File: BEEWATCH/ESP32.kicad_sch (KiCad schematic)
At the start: 34 parts, among them U4 W25Q128JVS

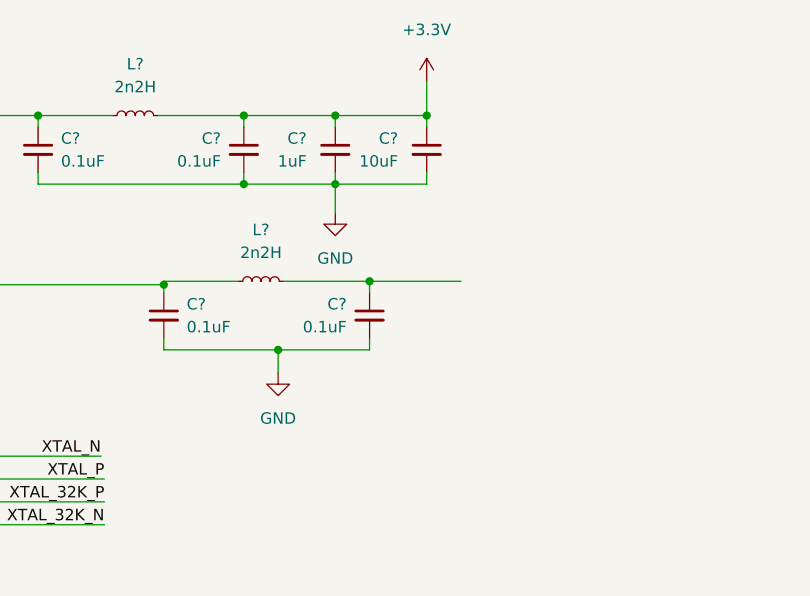
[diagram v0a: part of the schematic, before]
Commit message: Inverted F Antenna designed
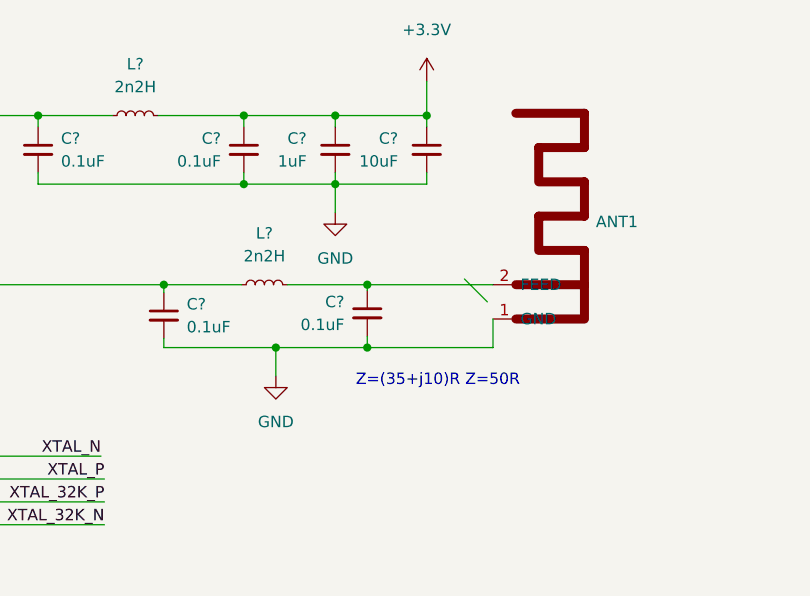
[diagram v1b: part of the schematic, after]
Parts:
- added ANT1: ~, Project:IFA_2.4GHz, symbol Project_Library:IFA_2.4GHz
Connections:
- net GND: now also ANT1.1 (GND)
- net at C?.1, L?.2: now also ANT1.2 (FEED)
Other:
- note added: "Z=(35+j10)R Z=50R"
- moved on the sheet: L?
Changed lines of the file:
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@@
   (junction (at 164.084 49.149) (diameter 0) (color 0 0 0 0)
   )
+  (junction (at 294.64 67.945) (diameter 0) (color 0 0 0 0)
+  )
   (junction (at 301.244 49.149) (diameter 0) (color 0 0 0 0)
   )
   (junction (at 258.064 49.149) (diameter 0) (color 0 0 0 0)
   )
+  (junction (at 294.64 74.93) (diameter 0) (color 0 0 0 0)
+  )
   (junction (at 355.854 225.171) (diameter 0) (color 0 0 0 0)
   )
@@
   (junction (at 58.42 120.015) (diameter 0) (color 0 0 0 0)
   )
+  (junction (at 284.48 74.93) (diameter 0) (color 0 0 0 0)
+  )
   (junction (at 349.25 206.756) (diameter 0) (color 0 0 0 0)
   )
@@
   (junction (at 234.95 49.149) (diameter 0) (color 0 0 0 0)
   )
-  (junction (at 294.894 67.564) (diameter 0) (color 0 0 0 0)
-  )
   (junction (at 184.404 49.149) (diameter 0) (color 0 0 0 0)
   )
@@
   (junction (at 280.924 49.149) (diameter 0) (color 0 0 0 0)
   )
-  (junction (at 284.734 75.184) (diameter 0) (color 0 0 0 0)
-  )
   (junction (at 58.42 114.935) (diameter 0) (color 0 0 0 0)
   )
@@
   (junction (at 174.244 49.149) (diameter 0) (color 0 0 0 0)
   )
+  (bus_entry (at 305.435 67.31) (size 2.54 2.54)
+    (stroke (width 0) (type default))
+  )
   (wire (pts (xy 223.52 127.635) (xy 223.52 125.095))
     (stroke (width 0) (type default))
@@
     (stroke (width 0) (type default))
   )
-  (wire (pts (xy 272.034 67.945) (xy 272.034 67.564))
-    (stroke (width 0) (type default))
-  )
   (wire (pts (xy 214.63 49.149) (xy 214.63 55.245))
     (stroke (width 0) (type default))
   )
-  (wire (pts (xy 294.894 68.834) (xy 294.894 67.564))
-    (stroke (width 0) (type default))
-  )
   (wire (pts (xy 183.515 71.755) (xy 192.405 71.755))
     (stroke (width 0) (type default))
@@
     (stroke (width 0) (type default))
   )
-  (wire (pts (xy 284.734 75.184) (xy 272.034 75.184))
-    (stroke (width 0) (type default))
-  )
   (wire (pts (xy 280.924 56.769) (xy 280.924 55.499))
     (stroke (width 0) (type default))
@@
     (stroke (width 0) (type default))
   )
+  (wire (pts (xy 308.61 74.93) (xy 294.64 74.93))
+    (stroke (width 0) (type default))
+  )
   (wire (pts (xy 349.885 170.815) (xy 349.885 179.07))
     (stroke (width 0) (type default))
@@
     (stroke (width 0) (type default))
   )
-  (wire (pts (xy 272.034 73.914) (xy 272.034 75.184))
+  (wire (pts (xy 272.034 73.914) (xy 272.034 74.93))
     (stroke (width 0) (type default))
   )
@@
     (stroke (width 0) (type default))
   )
-  (wire (pts (xy 284.734 75.184) (xy 284.734 77.724))
-    (stroke (width 0) (type default))
-  )
-  (wire (pts (xy 305.054 67.564) (xy 294.894 67.564))
+  (wire (pts (xy 284.48 74.93) (xy 284.48 78.105))
+    (stroke (width 0) (type default))
+  )
+  (wire (pts (xy 294.64 67.945) (xy 308.61 67.945))
     (stroke (width 0) (type default))
   )
@@
     (stroke (width 0) (type default))
   )
-  (wire (pts (xy 272.034 67.564) (xy 280.289 67.564))
+  (wire (pts (xy 272.034 67.945) (xy 280.67 67.945))
     (stroke (width 0) (type default))
   )
@@
     (stroke (width 0) (type default))
   )
-  (wire (pts (xy 294.894 67.564) (xy 285.369 67.564))
-    (stroke (width 0) (type default))
-  )
   (wire (pts (xy 197.485 66.675) (xy 198.12 66.675))
     (stroke (width 0) (type default))
@@
     (stroke (width 0) (type default))
   )
-  (wire (pts (xy 294.894 75.184) (xy 284.734 75.184))
+  (wire (pts (xy 294.64 74.93) (xy 284.48 74.93))
     (stroke (width 0) (type default))
   )
@@
     (stroke (width 0) (type default))
   )
+  (wire (pts (xy 308.61 71.755) (xy 308.61 74.93))
+    (stroke (width 0) (type default))
+  )
   (wire (pts (xy 361.95 183.515) (xy 361.95 189.103))
     (stroke (width 0) (type default))
@@
     (stroke (width 0) (type default))
   )
+  (wire (pts (xy 294.64 67.945) (xy 285.75 67.945))
+    (stroke (width 0) (type default))
+  )
   (wire (pts (xy 349.885 189.103) (xy 356.743 189.103))
     (stroke (width 0) (type default))
@@
     (stroke (width 0) (type default))
   )
-  (wire (pts (xy 294.894 75.184) (xy 294.894 73.914))
+  (wire (pts (xy 294.64 73.66) (xy 294.64 74.93))
+    (stroke (width 0) (type default))
+  )
+  (wire (pts (xy 294.64 67.945) (xy 294.64 68.58))
     (stroke (width 0) (type default))
   )
@@
   )
   (wire (pts (xy 280.924 56.769) (xy 258.064 56.769))
+    (stroke (width 0) (type default))
+  )
+  (wire (pts (xy 284.48 74.93) (xy 272.034 74.93))
     (stroke (width 0) (type default))
   )
@@
     (effects (font (size 1.27 1.27)) (justify left bottom))
   )
+  (text "Z=(35+j10)R Z=50R\n" (at 293.37 79.375 0)
+    (effects (font (size 1.27 1.27)) (justify left bottom))
+  )
   (label "SPI_D0" (at 183.515 69.215 0) (fields_autoplaced)
     (effects (font (size 1.27 1.27)) (justify left bottom))
@@
     (effects (font (size 1.27 1.27)) (justify right))
   )
-  (symbol (lib_id "Device:C_Small") (at 294.894 71.374 0) (mirror y) (unit 1)
-    (in_bom yes) (on_board yes) (dnp no) (fields_autoplaced)
-    (property "Reference" "C?" (at 292.354 70.1102 0)
-      (effects (font (size 1.27 1.27)) (justify left))
-    )
-    (property "Value" "0.1uF" (at 292.354 72.6502 0)
-      (effects (font (size 1.27 1.27)) (justify left))
-    )
-    (property "Footprint" "" (at 294.894 71.374 0)
-      (effects (font (size 1.27 1.27)) hide)
-    )
-    (property "Datasheet" "~" (at 294.894 71.374 0)
+  (symbol (lib_id "Device:C_Small") (at 294.64 71.12 0) (mirror y) (unit 1)
+    (in_bom yes) (on_board yes) (dnp no) (fields_autoplaced)
+    (property "Reference" "C?" (at 292.1 69.8562 0)
+      (effects (font (size 1.27 1.27)) (justify left))
+    )
+    (property "Value" "0.1uF" (at 292.1 72.3962 0)
+      (effects (font (size 1.27 1.27)) (justify left))
+    )
+    (property "Footprint" "" (at 294.64 71.12 0)
+      (effects (font (size 1.27 1.27)) hide)
+    )
+    (property "Datasheet" "~" (at 294.64 71.12 0)
       (effects (font (size 1.27 1.27)) hide)
     )
@@
     )
   )
-  (symbol (lib_id "Device:L_Small") (at 282.829 67.564 90) (unit 1)
-    (in_bom yes) (on_board yes) (dnp no) (fields_autoplaced)
-    (property "Reference" "L?" (at 282.829 61.849 90)
-      (effects (font (size 1.27 1.27)))
-    )
-    (property "Value" "2n2H" (at 282.829 64.389 90)
-      (effects (font (size 1.27 1.27)))
-    )
-    (property "Footprint" "" (at 282.829 67.564 0)
-      (effects (font (size 1.27 1.27)) hide)
-    )
-    (property "Datasheet" "~" (at 282.829 67.564 0)
+  (symbol (lib_id "Device:L_Small") (at 283.21 67.945 90) (unit 1)
+    (in_bom yes) (on_board yes) (dnp no) (fields_autoplaced)
+    (property "Reference" "L?" (at 283.21 62.23 90)
+      (effects (font (size 1.27 1.27)))
+    )
+    (property "Value" "2n2H" (at 283.21 64.77 90)
+      (effects (font (size 1.27 1.27)))
+    )
+    (property "Footprint" "" (at 283.21 67.945 0)
+      (effects (font (size 1.27 1.27)) hide)
+    )
+    (property "Datasheet" "~" (at 283.21 67.945 0)
       (effects (font (size 1.27 1.27)) hide)
     )
@@
         (path "/e9c5fb53-480b-4989-8495-a3341ee99514/56d77f8e-c069-456f-a514-fdde13f048cd"
           (reference "L2") (unit 1)
+        )
+      )
+    )
+  )
+  (symbol (lib_id "Project_Library:IFA_2.4GHz") (at 311.15 67.945 0) (unit 1)
+    (in_bom yes) (on_board yes) (dnp no) (fields_autoplaced)
+    (property "Reference" "ANT1" (at 320.04 60.96 0)
+      (effects (font (size 1.27 1.27)) (justify left))
+    )
+    (property "Value" "~" (at 311.15 67.945 0)
+      (effects (font (size 1.27 1.27)))
+    )
+    (property "Footprint" "Project:IFA_2.4GHz" (at 311.15 67.945 0)
+      (effects (font (size 1.27 1.27)) hide)
+    )
+    (property "Datasheet" "" (at 311.15 67.945 0)
+      (effects (font (size 1.27 1.27)) hide)
+    )
+    (pin "1")
+    (pin "2")
+    (instances
+      (project "BEEWATCH"
+        (path "/e9c5fb53-480b-4989-8495-a3341ee99514/56d77f8e-c069-456f-a514-fdde13f048cd"
+          (reference "ANT1") (unit 1)
         )
       )
@@
     )
   )
-  (symbol (lib_id "power:GND") (at 284.734 77.724 0) (mirror y) (unit 1)
-    (in_bom yes) (on_board yes) (dnp no) (fields_autoplaced)
-    (property "Reference" "#PWR?" (at 284.734 84.074 0)
-      (effects (font (size 1.27 1.27)) hide)
-    )
-    (property "Value" "GND" (at 284.734 82.804 0)
-      (effects (font (size 1.27 1.27)))
-    )
-    (property "Footprint" "" (at 284.734 77.724 0)
-      (effects (font (size 1.27 1.27)) hide)
-    )
-    (property "Datasheet" "" (at 284.734 77.724 0)
-      (effects (font (size 1.27 1.27)) hide)
-    )
+  (symbol (lib_id "power:GND") (at 284.48 78.105 0) (mirror y) (unit 1)
+    (in_bom yes) (on_board yes) (dnp no) (fields_autoplaced)
+    (property "Reference" "#PWR?" (at 284.48 84.455 0)
+      (effects (font (size 1.27 1.27)) hide)
+    )
+    (property "Value" "GND" (at 284.48 83.185 0)
+      (effects (font (size 1.27 1.27)))
+    )
+    (property "Footprint" "" (at 284.48 78.105 0)
+      (effects (font (size 1.27 1.27)) hide)
+    )
+    (property "Datasheet" "" (at 284.48 78.105 0)
+      (effects (font (size 1.27 1.27)) hide)
+    )
